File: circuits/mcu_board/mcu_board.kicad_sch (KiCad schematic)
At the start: 44 parts, among them J1 USB_B_Micro, J2 Conn_01x13_Pin, J3 Conn_01x03_Pin, SW1 SW_Push, SW10 SW_Push, SW11 SW_Push, SW12 SW_Push, SW13 SW_Push, SW2 SW_Push, SW3 SW_Push, SW4 SW_Push, SW5 SW_Push, SW6 SW_Push, SW7 SW_Push, SW8 SW_Push, SW9 SW_Push, U1 AMS1117-3.3, U4 STM32F302CCTx, Y1 8MHz

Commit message: MCU板layout完成
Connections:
- net BTN_DOWN: now also U4.22 (PB11); no longer U4.21 (PB10)
- net BTN_RIGHT: now also U4.21 (PB10); no longer U4.22 (PB11)
- net BTN_X: now also U4.43 (PB7); no longer U4.45 (PB8)
- net BTN_Y: now also U4.45 (PB8); no longer U4.43 (PB7)
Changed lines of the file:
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@@
+    (effects (font (size 1.27 1.27)) (justify left bottom))
+  )
+  (label "BTN_RIGHT" (at 209.55 124.46 0) (fields_autoplaced)
     (effects (font (size 1.27 1.27)) (justify left bottom))
   )
@@
     (effects (font (size 1.27 1.27)) (justify left bottom))
   )
-  (label "BTN_DOWN" (at 209.55 124.46 0) (fields_autoplaced)
-    (effects (font (size 1.27 1.27)) (justify left bottom))
-  )
   (label "RIGHT_X" (at 160.02 57.15 0) (fields_autoplaced)
     (effects (font (size 1.27 1.27)) (justify left bottom))
@@
     (effects (font (size 1.27 1.27)) (justify left bottom))
   )
-  (label "BTN_RIGHT" (at 209.55 127 0) (fields_autoplaced)
+  (label "BTN_Y" (at 209.55 119.38 0) (fields_autoplaced)
     (effects (font (size 1.27 1.27)) (justify left bottom))
   )
@@
     (effects (font (size 1.27 1.27)) (justify left bottom))
   )
-  (label "BTN_Y" (at 209.55 116.84 0) (fields_autoplaced)
-    (effects (font (size 1.27 1.27)) (justify left bottom))
-  )
   (label "PB1" (at 226.06 101.6 0) (fields_autoplaced)
     (effects (font (size 1.27 1.27)) (justify left bottom))
@@
     (effects (font (size 1.27 1.27)) (justify left bottom))
   )
-  (label "BTN_X" (at 209.55 119.38 0) (fields_autoplaced)
-    (effects (font (size 1.27 1.27)) (justify left bottom))
-  )
   (label "LEFT_X" (at 160.02 44.45 0) (fields_autoplaced)
     (effects (font (size 1.27 1.27)) (justify left bottom))
   )
   (label "BTN_DOWN" (at 129.2946 106.68 0) (fields_autoplaced)
+    (effects (font (size 1.27 1.27)) (justify left bottom))
+  )
+  (label "BTN_DOWN" (at 209.55 127 0) (fields_autoplaced)
     (effects (font (size 1.27 1.27)) (justify left bottom))
   )
@@
     (effects (font (size 1.27 1.27)) (justify left bottom))
   )
+  (label "BTN_X" (at 209.55 116.84 0) (fields_autoplaced)
+    (effects (font (size 1.27 1.27)) (justify left bottom))
+  )

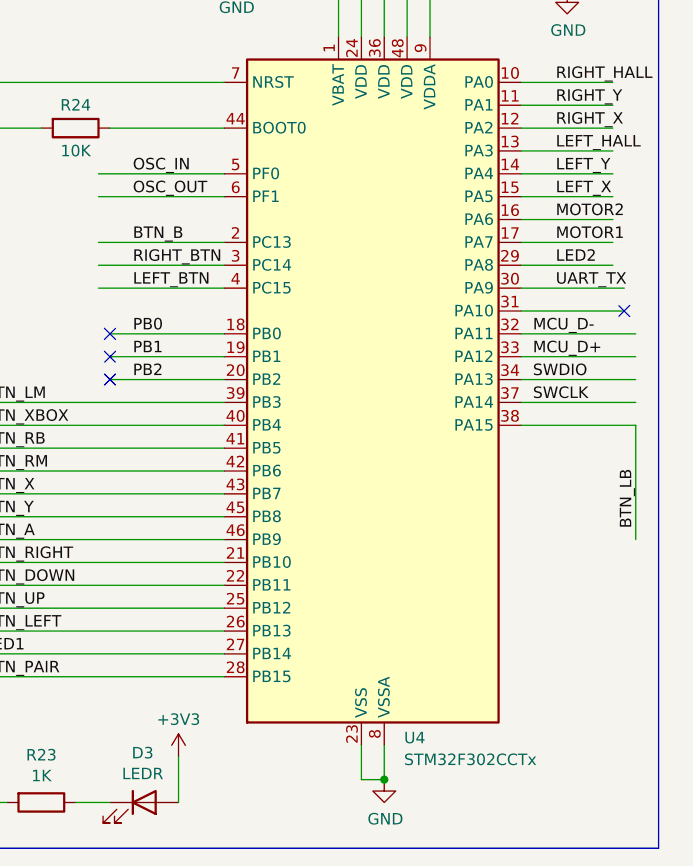
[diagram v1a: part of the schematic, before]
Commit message: 修改单片机型号
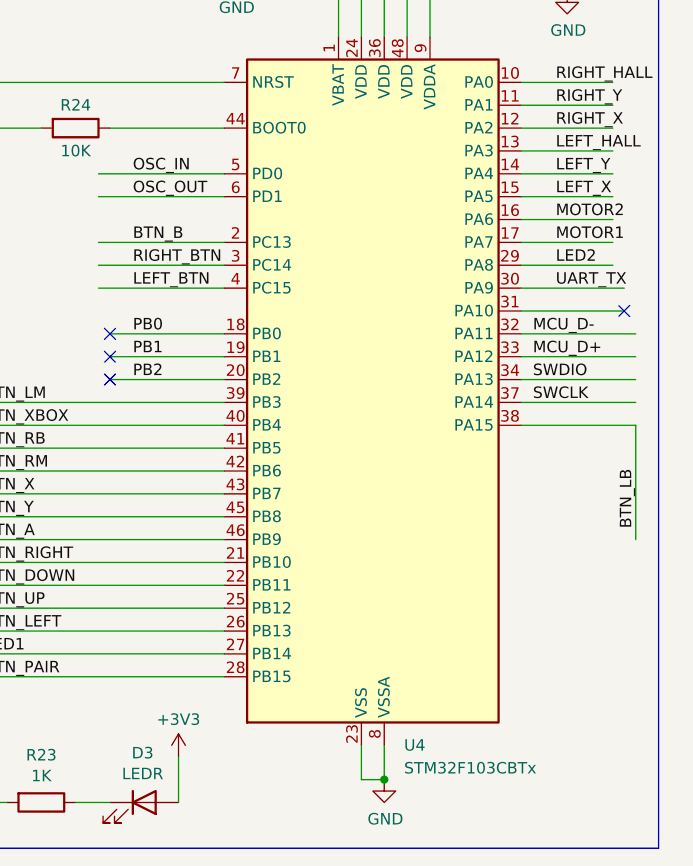
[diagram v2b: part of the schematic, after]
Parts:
- removed U4: STM32F302CCTx, Package_QFP:LQFP-48_7x7mm_P0.5mm, symbol MCU_ST_STM32F3:STM32F302CCTx
- added U4: STM32F103CBTx, Package_QFP:LQFP-48_7x7mm_P0.5mm, symbol MCU_ST_STM32F1:STM32F103CBTx
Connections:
- net +3V3: now also U4.1 (VBAT), U4.24 (VDD), U4.36 (VDD), U4.48 (VDD), U4.9 (VDDA)
- net BTN_A: now also U4.46 (PB9)
- net BTN_B: now also U4.2 (PC13)
- net BTN_DOWN: now also U4.22 (PB11)
- net BTN_LB: now also U4.38 (PA15)
- net BTN_LEFT: now also U4.26 (PB13)
- net BTN_LM: now also U4.39 (PB3)
- net BTN_PAIR: now also U4.28 (PB15)
- net BTN_RB: now also U4.41 (PB5)
- net BTN_RIGHT: now also U4.21 (PB10)
- net BTN_RM: now also U4.42 (PB6)
- net BTN_UP: now also U4.25 (PB12)
- net BTN_X: now also U4.43 (PB7)
- net BTN_XBOX: now also U4.40 (PB4)
- net BTN_Y: now also U4.45 (PB8)
- net GND: now also U4.23 (VSS), U4.35 (VSS), U4.47 (VSS), U4.8 (VSSA)
- net LED1: now also U4.27 (PB14)
- net LED2: now also U4.29 (PA8)
- net LEFT_BTN: now also U4.4 (PC15)
- net LEFT_HALL: now also U4.13 (PA3)
- net LEFT_X: now also U4.15 (PA5)
- net LEFT_Y: now also U4.14 (PA4)
- net MCU_D+: now also U4.33 (PA12)
- net MCU_D-: now also U4.32 (PA11)
- net MOTOR1: now also U4.17 (PA7)
- net MOTOR2: now also U4.16 (PA6)
- net OSC_IN: now also U4.5 (PD0)
- net OSC_OUT: now also U4.6 (PD1)
- net PB0: now also U4.18 (PB0)
- net PB1: now also U4.19 (PB1)
- net PB2: now also U4.20 (PB2)
- net RIGHT_BTN: now also U4.3 (PC14)
- net RIGHT_HALL: now also U4.10 (PA0)
- net RIGHT_X: now also U4.12 (PA2)
- net RIGHT_Y: now also U4.11 (PA1)
- net SWCLK: now also U4.37 (PA14)
- net SWDIO: now also U4.34 (PA13)
- net UART_TX: now also U4.30 (PA9)
- net at C6.1, R22.1: now also U4.7 (NRST)
- net at R24.1: now also U4.44 (BOOT0)
